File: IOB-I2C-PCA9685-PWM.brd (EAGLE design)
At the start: 71.1 x 33 mm, 12 parts, among them IC1 PCA9685PW, SW1 A0, SW2 A1

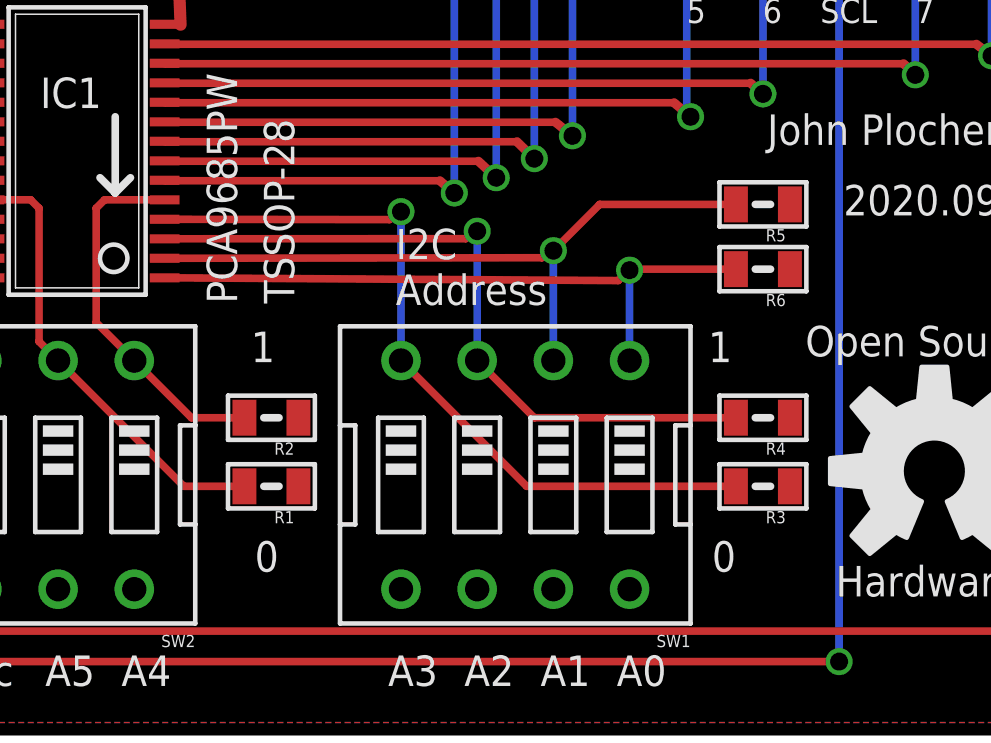
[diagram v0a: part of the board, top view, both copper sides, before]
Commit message: normalized values
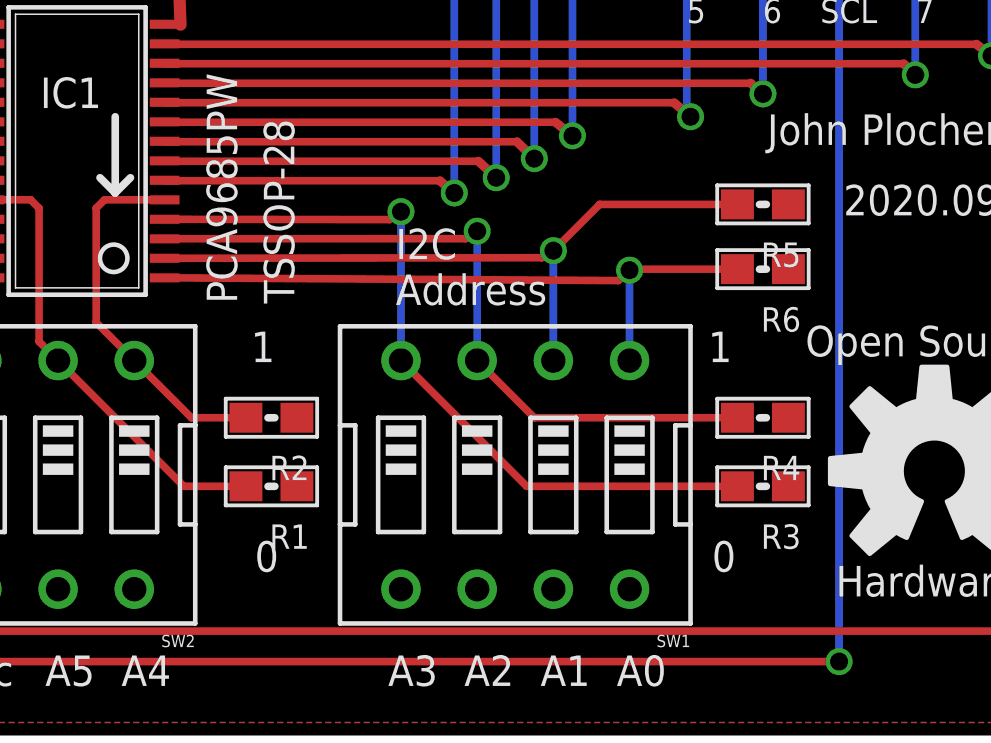
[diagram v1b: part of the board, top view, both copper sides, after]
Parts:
- R1, R2, R3, R4, R5, R6: device SPCoast:0805-RES -> SPCoast:0603-RES
- SW1: value A0 -> SPSTx4
- SW2: value A1 -> SPSTx4
- U$1: value DOC-OSHW-LOGO-L -> OSHW
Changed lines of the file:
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@@
 <setting verticaltext="up"/>
 </settings>
-<grid distance="50" unitdist="mil" unit="mil" style="dots" multiple="2" display="yes" altdistance="5" altunitdist="mil" altunit="mil"/>
+<grid distance="50" unitdist="mil" unit="mil" style="dots" multiple="2" display="yes" altdistance="25" altunitdist="mil" altunit="mil"/>
 <layers>
 <layer number="1" name="Top" color="4" fill="1" visible="yes" active="yes"/>
@@
 </autorouter>
 <elements>
-<element name="U$1" library="SPCoast" package="OSHW-LOGO-L" value="DOC-OSHW-LOGO-L" x="64.135" y="9.017" smashed="yes"/>
-<element name="SW1" library="SPCoast" package="EDG-04" value="A0" x="50.165" y="8.89" smashed="yes" rot="R180">
+<element name="U$1" library="SPCoast" package="OSHW-LOGO-L" value="OSHW" x="64.135" y="9.017" smashed="yes"/>
+<element name="SW1" library="SPCoast" package="EDG-04" value="SPSTx4" x="50.165" y="8.89" smashed="yes" rot="R180">
 <attribute name="VALUE" x="56.007" y="15.494" size="0.4064" layer="27" ratio="10" rot="R180"/>
 <attribute name="NAME" x="56.007" y="3.556" size="0.4064" layer="25" ratio="10" rot="R180"/>
 </element>
-<element name="SW2" library="SPCoast" package="EDG-04" value="A1" x="33.655" y="8.89" smashed="yes" rot="R180">
+<element name="SW2" library="SPCoast" package="EDG-04" value="SPSTx4" x="33.655" y="8.89" smashed="yes" rot="R180">
 <attribute name="VALUE" x="39.497" y="15.494" size="0.4064" layer="27" ratio="10" rot="R180"/>
 <attribute name="NAME" x="39.497" y="3.556" size="0.4064" layer="25" ratio="10" rot="R180"/>
@@
 <attribute name="VALUE" x="40.894" y="14.605" size="1.016" layer="27" ratio="10" rot="R90"/>
 </element>
-<element name="R1" library="SPCoast" package="0805-RES" value="10k" x="42.037" y="8.509" rot="R180"/>
-<element name="R2" library="SPCoast" package="0805-RES" value="10k" x="42.037" y="10.795" rot="R180"/>
-<element name="R3" library="SPCoast" package="0805-RES" value="10k" x="58.42" y="8.509" rot="R180"/>
-<element name="R4" library="SPCoast" package="0805-RES" value="10k" x="58.42" y="10.795" rot="R180"/>
-<element name="R5" library="SPCoast" package="0805-RES" value="10k" x="58.42" y="17.907" rot="R180"/>
-<element name="R6" library="SPCoast" package="0805-RES" value="10k" x="58.42" y="15.748" rot="R180"/>
+<element name="R1" library="SPCoast" package="0603-RES" value="10k" x="42.037" y="8.509" rot="R180"/>
+<element name="R2" library="SPCoast" package="0603-RES" value="10k" x="42.037" y="10.795" rot="R180"/>
+<element name="R3" library="SPCoast" package="0603-RES" value="10k" x="58.42" y="8.509" rot="R180"/>
+<element name="R4" library="SPCoast" package="0603-RES" value="10k" x="58.42" y="10.795" rot="R180"/>
+<element name="R5" library="SPCoast" package="0603-RES" value="10k" x="58.42" y="17.907" rot="R180"/>
+<element name="R6" library="SPCoast" package="0603-RES" value="10k" x="58.42" y="15.748" rot="R180"/>
 </elements>
 <signals>
@@
 <via x="48.895" y="17.014" extent="1-16" drill="0.6"/>
 <contactref element="R4" pad="2"/>
-<wire x1="57.52" y1="10.795" x2="50.8" y2="10.795" width="0.254" layer="1"/>
+<wire x1="57.57" y1="10.795" x2="50.8" y2="10.795" width="0.254" layer="1"/>
 <wire x1="50.8" y1="10.795" x2="48.895" y2="12.7" width="0.254" layer="1"/>
 </signal>
@@
 <via x="51.435" y="16.364" extent="1-16" drill="0.6"/>
 <contactref element="R5" pad="2"/>
-<wire x1="57.52" y1="17.907" x2="52.978" y2="17.907" width="0.254" layer="1"/>
+<wire x1="57.57" y1="17.907" x2="52.978" y2="17.907" width="0.254" layer="1"/>
 <wire x1="52.978" y1="17.907" x2="51.435" y2="16.364" width="0.254" layer="1"/>
 </signal>
@@
 <via x="53.975" y="15.714" extent="1-16" drill="0.6"/>
 <contactref element="R6" pad="2"/>
-<wire x1="57.52" y1="15.748" x2="54.009" y2="15.748" width="0.254" layer="1"/>
+<wire x1="57.57" y1="15.748" x2="54.009" y2="15.748" width="0.254" layer="1"/>
 <wire x1="54.009" y1="15.748" x2="53.975" y2="15.714" width="0.254" layer="1"/>
 </signal>
@@
 <via x="46.355" y="17.664" extent="1-16" drill="0.6"/>
 <contactref element="R3" pad="2"/>
-<wire x1="57.52" y1="8.509" x2="50.546" y2="8.509" width="0.254" layer="1"/>
+<wire x1="57.57" y1="8.509" x2="50.546" y2="8.509" width="0.254" layer="1"/>
 <wire x1="50.546" y1="8.509" x2="46.355" y2="12.7" width="0.254" layer="1"/>
 </signal>
@@
 <contactref element="R2" pad="2"/>
 <wire x1="37.465" y1="12.7" x2="39.37" y2="10.795" width="0.254" layer="1"/>
-<wire x1="39.37" y1="10.795" x2="41.137" y2="10.795" width="0.254" layer="1"/>
+<wire x1="39.37" y1="10.795" x2="41.187" y2="10.795" width="0.254" layer="1"/>
 </signal>
 <signal name="A5">
@@
 <contactref element="R1" pad="2"/>
 <wire x1="34.925" y1="12.7" x2="39.116" y2="8.509" width="0.254" layer="1"/>
-<wire x1="39.116" y1="8.509" x2="41.137" y2="8.509" width="0.254" layer="1"/>
+<wire x1="39.116" y1="8.509" x2="41.187" y2="8.509" width="0.254" layer="1"/>
 </signal>
 </signals>
